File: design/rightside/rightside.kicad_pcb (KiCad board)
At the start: 4 copper layers, 142.6 x 96.2 mm, 227 parts, among them IC2 XC9148G50CER-G, IC3 nRF52833-QDAA-R7, IC4 74AHCT125PW,118, IC5 MCP23018T-E_SS, IC6 XC9291B33D1R-G, J1 USB_C_Receptacle_USB2.0_16P, J2 Battery Pos, J3 Battery Neg, J4 OLED_128x32, J6 Conn_01x04, J7 F32Q-1A7H1-11012, U1 BQ27441-G1, U2 BQ24072RGT, U3 USB6B1, U5 PEC11L-4015F-S0015, U6 PEC11L-4015F-S0015, Y1 ECS-320-8-37B2-JTY-TR

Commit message: RS LS Complete
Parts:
- removed the REF** at (316.4, 158.4)
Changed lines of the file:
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@@
 		(pad_to_mask_clearance 0)
 		(allow_soldermask_bridges_in_footprints no)
-		(grid_origin 130.6005 39.6434)
+		(grid_origin 236.160969 76.380719)
 		(pcbplotparams
 			(layerselection 0x00010fc_ffffffff)
@@
 		)
 	)
-	(footprint "CustomLibrary:M1.6 Hole"
-		(layer "F.Cu")
-		(at 316.360969 158.380719)
-		(property "Reference" "REF**"
-			(at 0 -2 0)
-			(unlocked yes)
-			(layer "F.SilkS")
-			(hide yes)
-			(effects
-				(font
-					(size 1 1)
-					(thickness 0.1)
-				)
-			)
-		)
-		(property "Value" "M1.6 Hole"
-			(at 0 1 0)
-			(unlocked yes)
-			(layer "F.Fab")
-			(hide yes)
-			(effects
-				(font
-					(size 1 1)
-					(thickness 0.15)
-				)
-			)
-		)
-		(property "Footprint" "CustomLibrary:M1.6 Hole"
-			(at 2.4 -0.1 0)
-			(unlocked yes)
-			(layer "F.Fab")
-			(hide yes)
-			(effects
-				(font
-					(size 1 1)
-					(thickness 0.15)
-				)
-			)
-		)
-		(property "Datasheet" ""
-			(at 2.4 -0.1 0)
-			(unlocked yes)
-			(layer "F.Fab")
-			(hide yes)
-			(effects
-				(font
-					(size 1 1)
-					(thickness 0.15)
-				)
-			)
-		)
-		(property "Description" ""
-			(at 2.4 -0.1 0)
-			(unlocked yes)
-			(layer "F.Fab")
-			(hide yes)
-			(effects
-				(font
-					(size 1 1)
-					(thickness 0.15)
-				)
-			)
-		)
-		(attr through_hole)
-		(fp_circle
-			(center 0 0)
-			(end 1.3 0)
-			(stroke
-				(width 0.15)
-				(type solid)
-			)
-			(fill none)
-			(layer "Cmts.User")
-		)
-		(fp_circle
-			(center 0 0)
-			(end 1.5 0)
-			(stroke
-				(width 0.05)
-				(type solid)
-			)
-			(fill none)
-			(layer "F.CrtYd")
-		)
-		(fp_text user "${REFERENCE}"
-			(at 0 2.5 0)
-			(unlocked yes)
-			(layer "F.Fab")
-			(hide yes)
-			(effects
-				(font
-					(size 1 1)
-					(thickness 0.15)
-				)
-			)
-		)
-		(pad "" np_thru_hole circle
-			(at 0 0)
-			(size 1.7 1.7)
-			(drill 1.7)
-			(layers "F&B.Cu" "*.Mask")
-		)
-	)
 	(footprint "ScottoKeebs_Components:LED_SK6812MINI"
 		(layer "F.Cu")
@@
 		(tags "Choc Keyswitch Switch CPG1350 V1 CPG1353 V2 Hotswap Plated Cutout Keycap 1.00u")
 		(property "Reference" "S1"
-			(at 0.7 -9.14 0)
+			(at 3.639531 -8.587319 0)
 			(layer "F.SilkS")
 			(effects
@@
 		(tags "Choc Keyswitch Switch CPG1350 V1 CPG1353 V2 Hotswap Plated Cutout Keycap 1.00u")
 		(property "Reference" "S3"
-			(at 0 -9 0)
+			(at -3.460469 -8.387319 0)
 			(layer "F.SilkS")
 			(effects
@@
 		(tags "Choc Keyswitch Switch CPG1350 V1 CPG1353 V2 Hotswap Plated Cutout Keycap 1.00u")
 		(property "Reference" "S4"
-			(at 0 -9 0)
+			(at 3.939531 -8.487319 0)
 			(layer "F.SilkS")
 			(effects
@@
 	)
 	(via
-		(at 241.456261 102.837639)
-		(size 0.6)
-		(drill 0.3)
+		(at 241.3505 102.6934)
+		(size 1)
+		(drill 0.8)
 		(layers "F.Cu" "B.Cu")
 		(net 2)
@@
 	)
 	(segment
+		(start 241.3505 102.6934)
+		(end 241.3505 103.1934)
+		(width 0.5)
+		(layer "B.Cu")
+		(net 2)
+	)
+	(segment
 		(start 274.882453 162.475353)
 		(end 275.697819 163.290719)
@@
 	)
 	(segment
-		(start 241.456261 102.837639)
-		(end 241.456261 102.426011)
+		(start 257.650969 160.670719)
+		(end 257.650969 161.544719)
 		(width 0.5)
 		(layer "B.Cu")
@@
 	)
 	(segment
-		(start 257.650969 160.670719)
-		(end 257.650969 161.544719)
+		(start 241.3505 102.6934)
+		(end 241.3505 102.32025)
 		(width 0.5)
 		(layer "B.Cu")
@@
 	)
 	(segment
-		(start 241.456261 102.837639)
-		(end 241.456261 103.299161)
-		(width 0.5)
-		(layer "B.Cu")
-		(net 2)
-	)
-	(segment
 		(start 253.410969 129.355719)
 		(end 251.885969 129.355719)
@@
 	)
 	(segment
+		(start 241.3505 102.32025)
+		(end 240.610969 101.580719)
+		(width 0.5)
+		(layer "B.Cu")
+		(net 2)
+	)
+	(segment
 		(start 242.060969 101.580719)
 		(end 242.648469 101.580719)
@@
 	)
 	(segment
+		(start 241.3505 103.1934)
+		(end 241.8005 103.6434)
+		(width 0.5)
+		(layer "B.Cu")
+		(net 2)
+	)
+	(segment
 		(start 275.697819 163.290719)
 		(end 276.930969 163.290719)
@@
 	)
 	(segment
-		(start 241.456261 102.426011)
-		(end 240.610969 101.580719)
-		(width 0.5)
-		(layer "B.Cu")
-		(net 2)
-	)
-	(segment
 		(start 240.360969 102.400719)
 		(end 240.110969 102.150719)
@@
 	)
 	(segment
-		(start 241.456261 103.299161)
-		(end 241.8005 103.6434)
-		(width 0.5)
-		(layer "B.Cu")
-		(net 2)
-	)
-	(segment
 		(start 240.010969 141.530719)
 		(end 240.010969 142.380719)
@@
 	)
 	(segment
-		(start 241.6505 104.8934)
-		(end 241.6505 108.320719)
-		(width 0.5)
-		(layer "F.Cu")
-		(net 3)
-	)
-	(segment
 		(start 284.220969 79.780719)
 		(end 283.530969 79.090719)
@@
 	)
 	(segment
+		(start 239.806756 103.149656)
+		(end 241.6505 104.9934)
+		(width 0.8)
+		(layer "F.Cu")
+		(net 3)
+	)
+	(segment
 		(start 251.235969 81.580719)
 		(end 251.235969 80.505719)
@@
 	)
 	(segment
+		(start 239.806756 97.661284)
+		(end 239.806756 103.149656)
+		(width 0.8)
+		(layer "F.Cu")
+		(net 3)
+	)
+	(segment
 		(start 241.5005 108.3684)
 		(end 240.9505 108.3684)
@@
 	)
 	(segment
-		(start 239.806756 97.661284)
-		(end 239.806756 103.049656)
-		(width 0.5)
-		(layer "F.Cu")
-		(net 3)
-	)
-	(segment
 		(start 380.810969 140.580719)
 		(end 380.810969 141.555719)
@@
 	)
 	(segment
-		(start 239.806756 103.049656)
-		(end 241.6505 104.8934)
-		(width 0.5)
-		(layer "F.Cu")
-		(net 3)
-	)
-	(segment
 		(start 253.560969 173.630719)
 		(end 252.275425 173.630719)
@@
 	)
 	(segment
+		(start 241.6505 104.9934)
+		(end 241.6505 108.320719)
+		(width 0.8)
+		(layer "F.Cu")
+		(net 3)
+	)
+	(segment
 		(start 380.810969 141.555719)
 		(end 380.760969 141.605719)
@@
 	)
 	(segment
-		(start 258.230969 158.420719)
-		(end 261.520969 158.420719)
+		(start 256.900969 164.160719)
+		(end 256.900969 159.750719)
 		(width 0.2)
 		(layer "F.Cu")
@@
 	)
 	(segment
-		(start 261.520969 158.420719)
-		(end 261.600969 158.500719)
+		(start 258.230969 158.420719)
+		(end 261.520969 158.420719)
 		(width 0.2)
 		(layer "F.Cu")
@@
 	)
 	(segment
-		(start 256.900969 164.160719)
-		(end 256.900969 159.750719)
+		(start 261.520969 158.420719)
+		(end 261.600969 158.500719)
 		(width 0.2)
 		(layer "F.Cu")
@@
 	)
 	(segment
-		(start 257.000969 164.260719)
+		(start 257.192075 164.451825)
 		(end 256.900969 164.160719)
 		(width 0.2)
@@
 	)
 	(via
-		(at 257.000969 164.260719)
+		(at 257.192075 164.451825)
 		(size 0.45)
 		(drill 0.3)
@@
 	)
 	(segment
-		(start 257.000969 164.260719)
+		(start 257.192075 164.451825)
 		(end 257.319969 164.579719)
 		(width 0.2)

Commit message: create first merged gerber, prepare to fix board outline
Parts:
- moved C1 229.7 mm to (38.3, 96.0)
- moved J4 229.7 mm to (56.8, 110.5)
- moved 3V3_2 229.7 mm to (43.1, 98.5)
- moved 3v3_1 229.7 mm to (20.0, 75.5)
- moved 5V_2 229.7 mm to (144.8, 76.4)
- moved 5V_3 229.7 mm to (96.3, 47.5)
- moved 5V_4 229.7 mm to (64.3, 19.7)
- moved ANT1 229.7 mm to (22.2, 113.2)
- moved C10 229.7 mm to (26.7, 27.3)
- moved C11 229.7 mm to (36.4, 109.3)
- moved C15 229.7 mm to (29.1, 107.7)
- moved C16 229.7 mm to (33.1, 104.6)
- moved C17 229.7 mm to (88.6, 103.5)
- moved C19 229.7 mm to (28.6, 102.4)
- moved C2 229.7 mm to (47.8, 107.3)
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
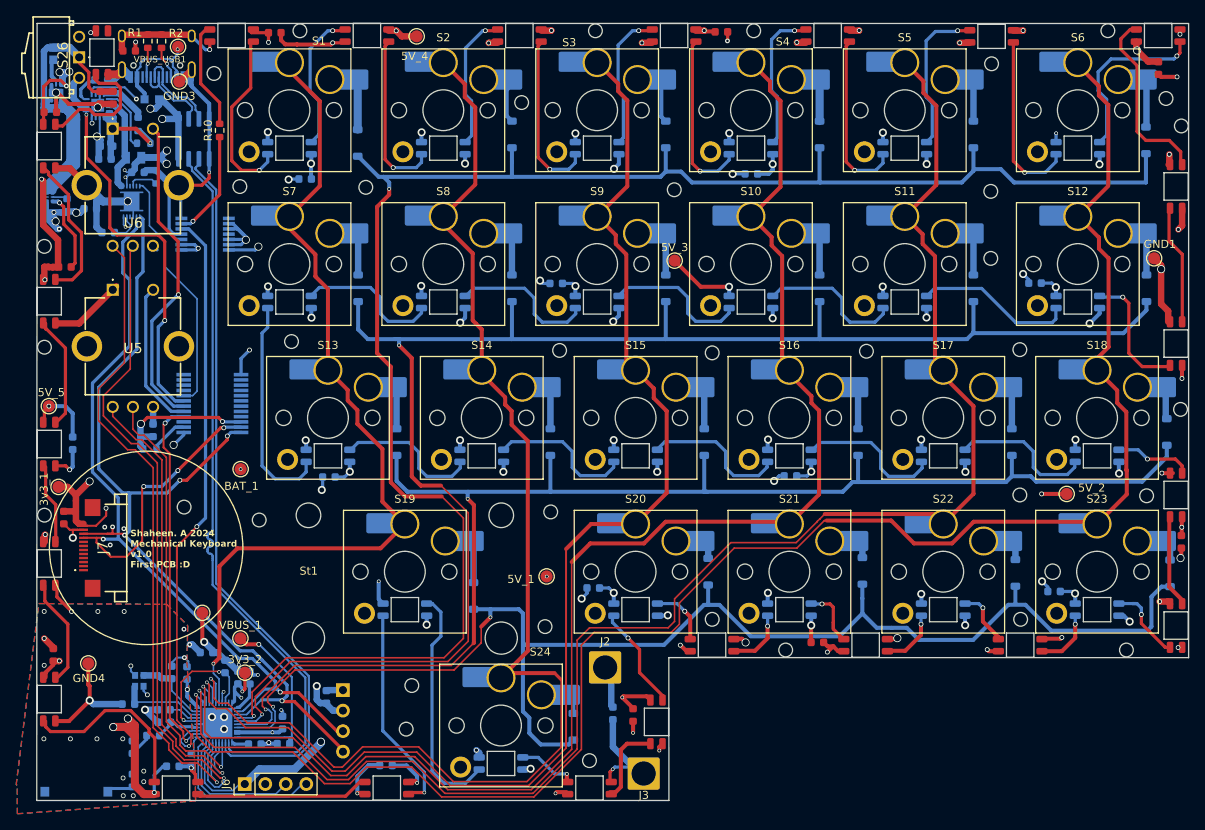
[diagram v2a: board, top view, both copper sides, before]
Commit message: submit merged design and do proper outline for boards
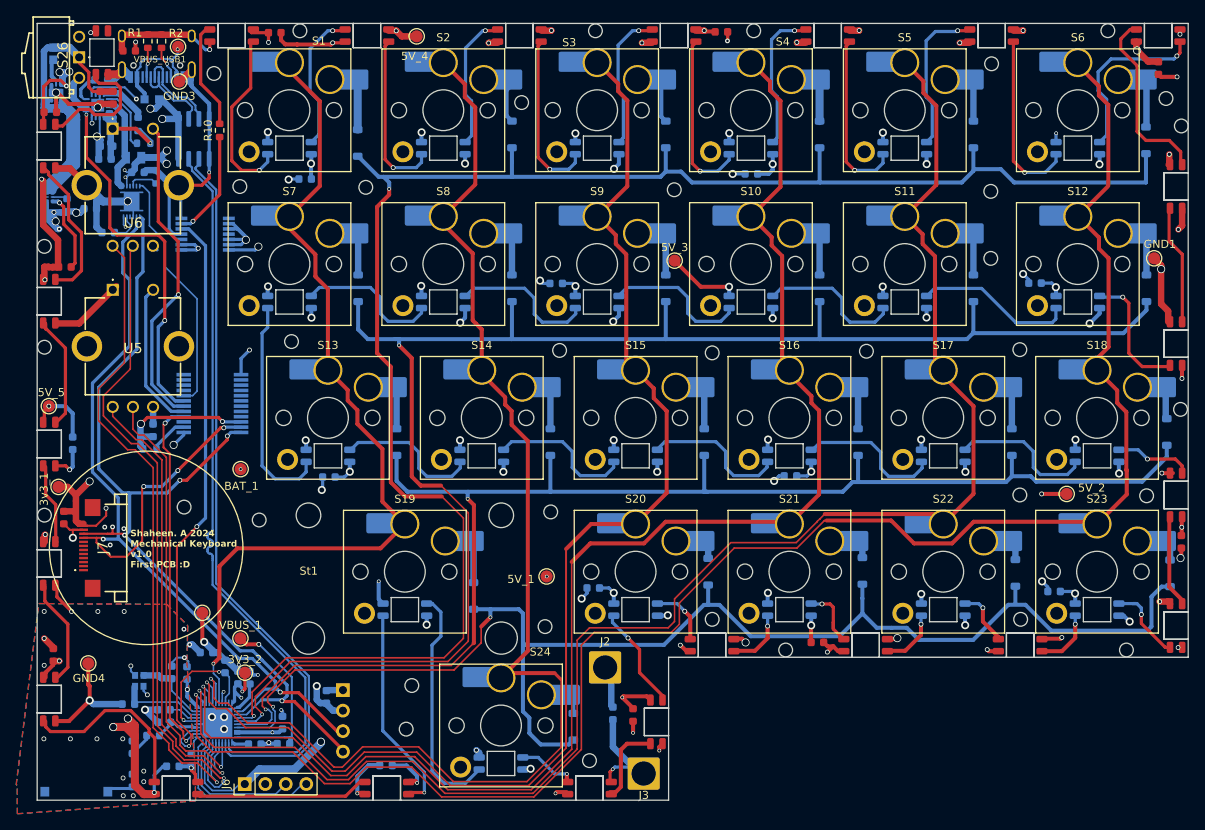
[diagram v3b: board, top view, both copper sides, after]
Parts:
- moved D11 0.10 mm to (135.5, 19.6)
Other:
- outline, holes or cut-outs redrawn
